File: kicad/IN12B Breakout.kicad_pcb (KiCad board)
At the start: 2 copper layers, 36.1 x 50.8 mm, 1 part

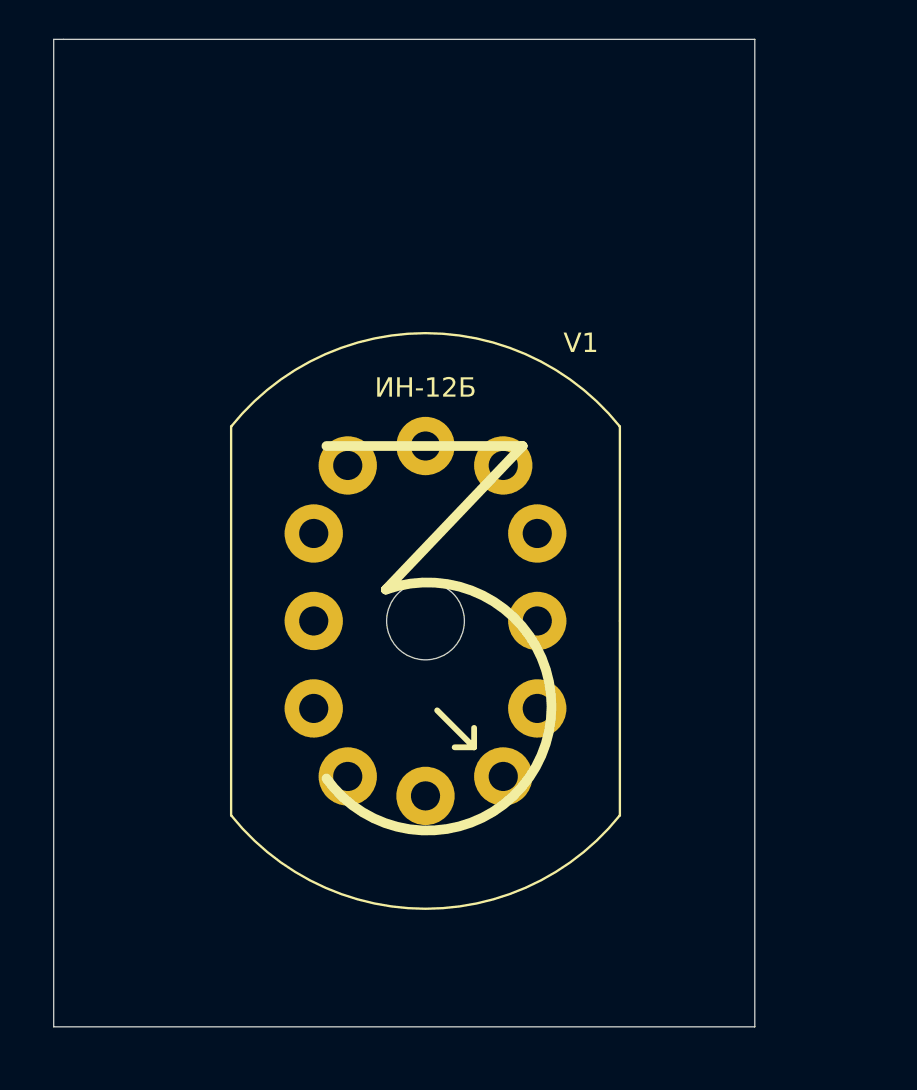
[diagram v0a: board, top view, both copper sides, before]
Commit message: IN12-B breakout
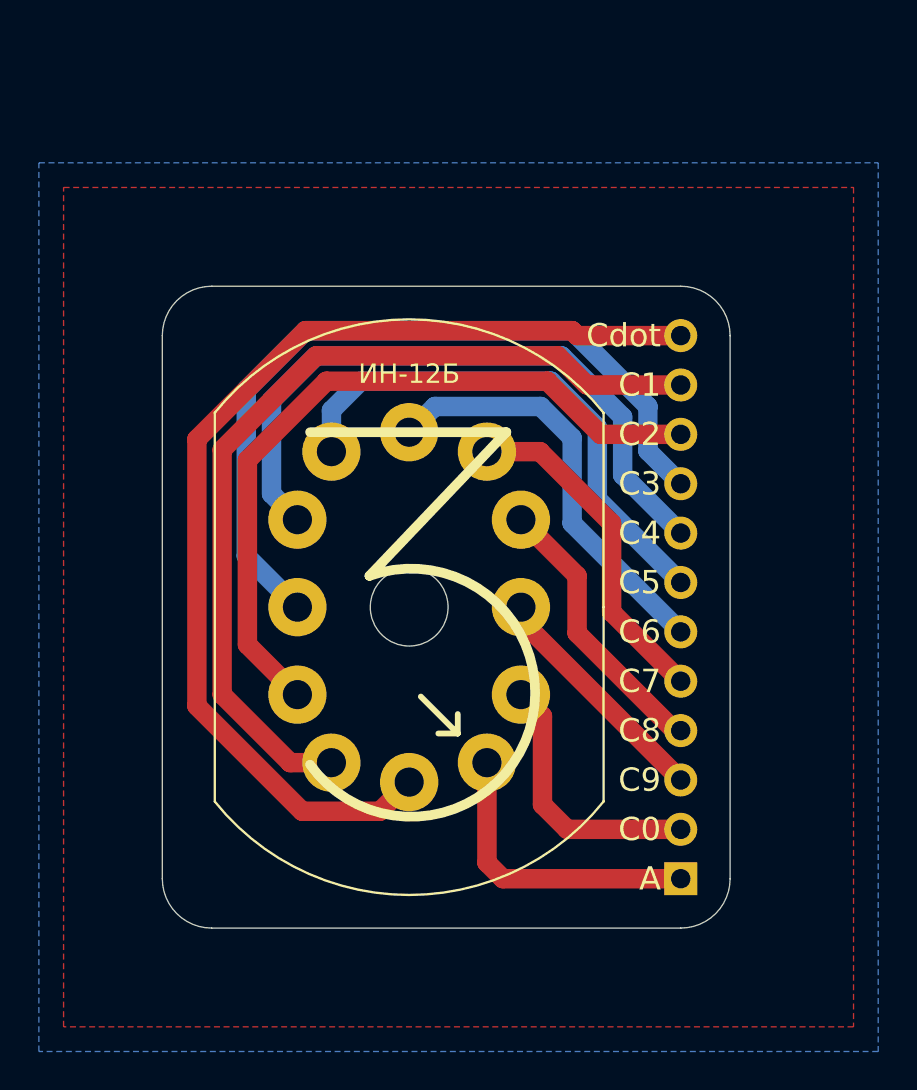
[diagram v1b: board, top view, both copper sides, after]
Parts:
- added G***: LOGO, barn53-kicad:cccp, B.Cu at (107.7, 47.9)
- added J1: Conn_01x12_Male, Connector_PinHeader_2.54mm:PinHeader_1x12_P2.54mm_Vertical, B.Cu at (113.0, 73.7)
- moved V1 1.10 mm to (99.1, 59.7)
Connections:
- V1 pad 1: (no net) -> /A
- V1 pad 10: (no net) -> /C2
- V1 pad 11: (no net) -> /C1
- V1 pad 12: (no net) -> /CDot
- V1 pad 2: (no net) -> /C0
- V1 pad 3: (no net) -> /C9
- V1 pad 4: (no net) -> /C8
- V1 pad 5: (no net) -> /C7
- V1 pad 6: (no net) -> /C6
- V1 pad 7: (no net) -> /C5
- V1 pad 8: (no net) -> /C4
- V1 pad 9: (no net) -> /C3
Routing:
- net /CDot: track 0.00 -> 54.8 mm
- net /C1: track 0.00 -> 45.9 mm
- net /C3: track 0.00 -> 40.5 mm
- net /C2: track 0.00 -> 38.2 mm
- net /C4: track 0.00 -> 34.2 mm
- net /C5: track 0.00 -> 27.2 mm
- net /C6: track 0.00 -> 21.9 mm
- net /C7: track 0.00 -> 17.5 mm
- net /A: track 0.00 -> 15.5 mm
- net /C8: track 0.00 -> 14.4 mm
- net /C0: track 0.00 -> 13.8 mm
- net /C9: track 0.00 -> 12.3 mm
- added copper zone on B.Cu, net (none)
- added copper zone on F.Cu, net (none)
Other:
- board size 36.1 x 50.8 mm -> 29.2 x 33 mm
- net class Default: clearance 0.127 -> 0.3; trace_width 0.1524 -> 1
- rule trace_clearance: 0.127 -> 0.3
- board text added: "A"
- board text added: "C0"
- board text added: "C1"
- board text added: "C2"
- board text added: "C3"
- board text added: "C4"
- board text added: "C5"
- board text added: "C6"
- board text added: "C7"
- board text added: "C8"
- board text added: "C9"
- board text added: "Cdot"
- board text added: "rev.A 07/21"
- board text added: "ИН-12Б NIXIE Breakout barn53.de"

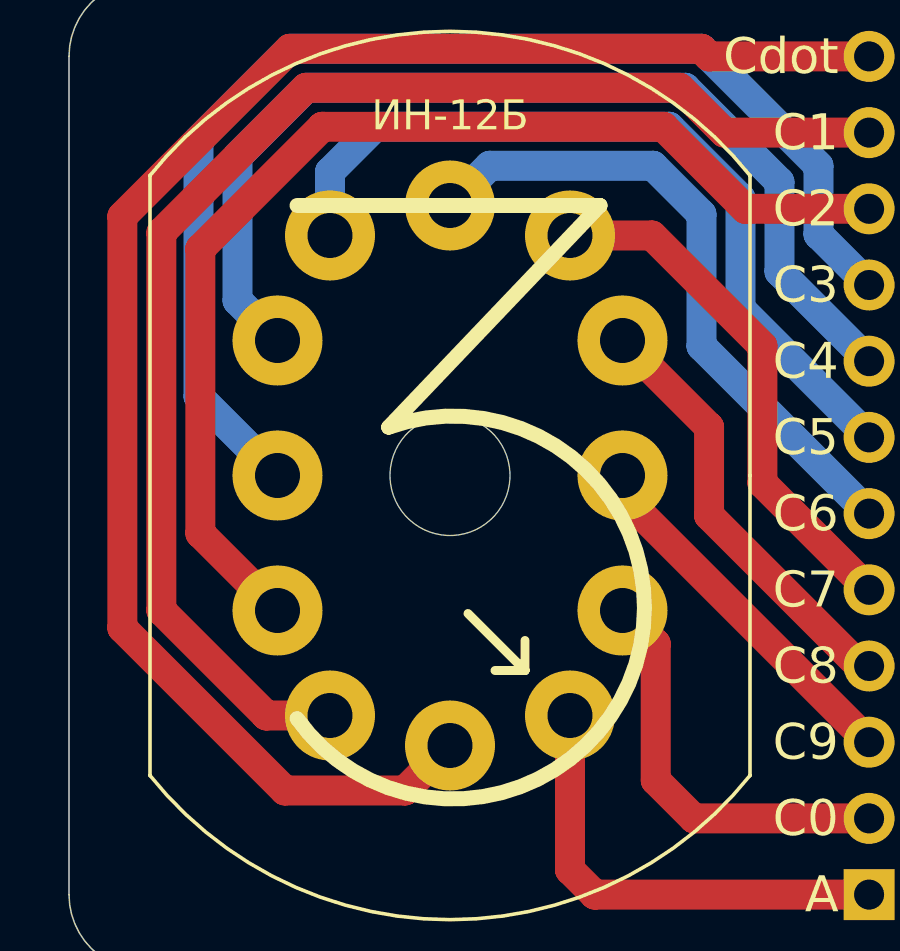
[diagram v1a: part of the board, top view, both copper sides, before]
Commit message: 1.7 mm nixie holes
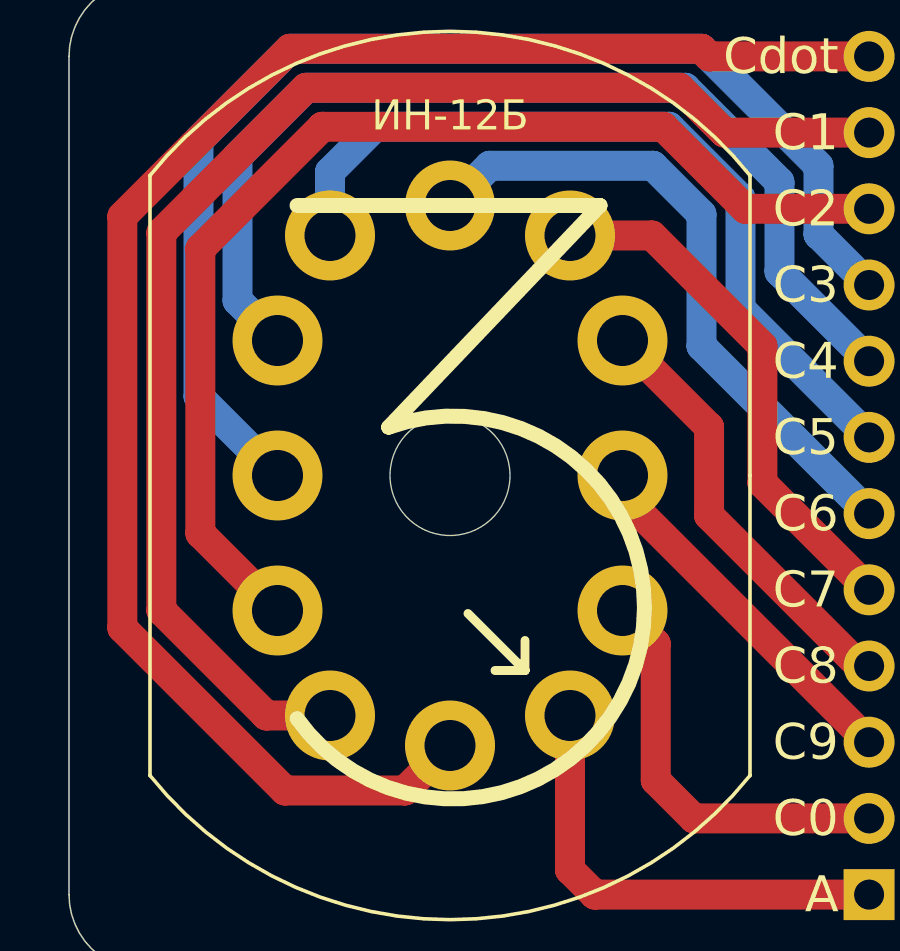
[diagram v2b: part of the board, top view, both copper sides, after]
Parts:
- V1: footprint barn53-kicad:IN12-B -> barn53-kicad:IN12-B-1.7mm
